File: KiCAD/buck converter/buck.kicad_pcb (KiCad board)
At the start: 2 copper layers, 42.2 x 24.9 mm, 17 parts, among them P1 VIN, P2 VOUT, Q1 Q_PMOS_DGS, U1 LTC1771

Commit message: Updated schematic, PCB, amd BOM
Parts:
- removed JP1: BURST, Connectors:PINHEAD1-3
- removed Q1: Q_PMOS_DGS, TO_SOT_Packages_SMD:SOT-23-6_Handsoldering
- added U2: SI3421DV-T1-GE3, TO_SOT_Packages_SMD:SOT-23-6_Handsoldering, F.Cu at (134.4, 95.2)
- C4: value 150uF -> 330uF; footprint Capacitors_SMD:CP_Elec_6.3x5.8 -> Capacitors_SMD:CP_Elec_8x10
- D2: footprint Diodes_SMD:D_SOD-323_HandSoldering -> Diodes_SMD:D_SMA_Handsoldering
- moved C3 10.5 mm to (133.6, 107.9)
- moved R2 10.5 mm to (131.4, 108.0)
- moved R4 10.5 mm to (135.9, 108.0)
- moved C4 8.15 mm to (124.0, 109.2), turned to 0 degrees
- moved C2 7.57 mm to (136.1, 102.6)
- moved P1 7.42 mm to (113.3, 102.6)
- moved R1 7.23 mm to (127.5, 96.0)
- moved C5 6.60 mm to (126.5, 94.0)
- moved C6 6.42 mm to (118.2, 93.5)
- moved C1 3.44 mm to (125.5, 103.6)
- moved D2 2.90 mm to (133.1, 90.9), turned to 180 degrees
- moved R3 1.27 mm to (134.6, 102.2)
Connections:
- U1 pad 8: /MODE -> GND
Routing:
- net GND: track 21.8 -> 47.1 mm, vias 5 -> 4
- net /MODE: track 19.2 -> 0.00 mm, vias 2 -> 0
- net Vfb: track 22.2 -> 8.71 mm, vias 2 -> 0
- net /Ith: track 12.7 -> 5.87 mm
- net Net-(C2-Pad1): track 9.40 -> 2.85 mm, vias 2 -> 0
- net /SENSE: track 19.9 -> 14.5 mm, vias 3 -> 2
- net /RUN/SS: track 6.06 -> 2.19 mm
- net /GATE: track 5.61 -> 2.20 mm
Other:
- board text removed: "-"

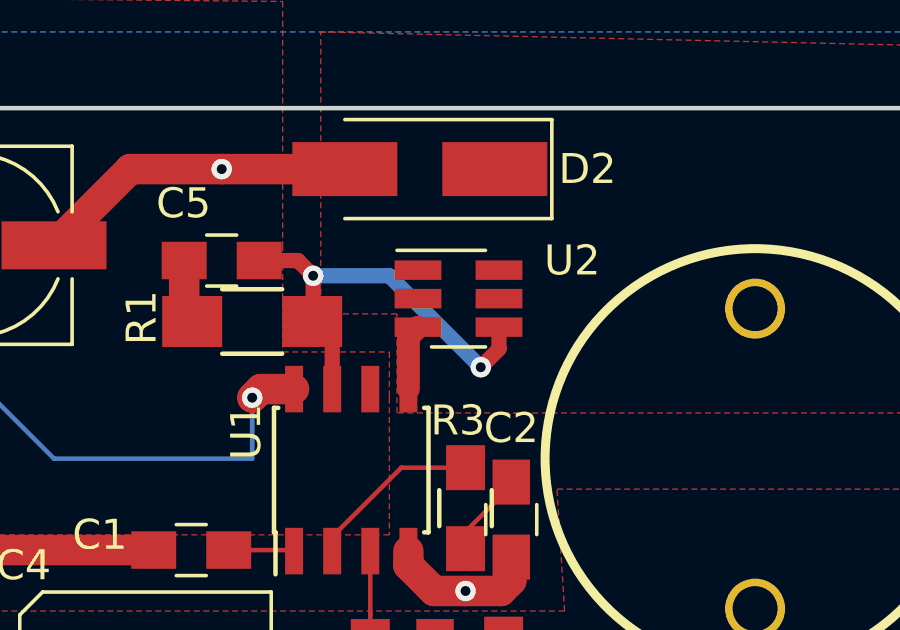
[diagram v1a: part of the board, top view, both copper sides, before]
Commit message: Updated PCB and SPICE
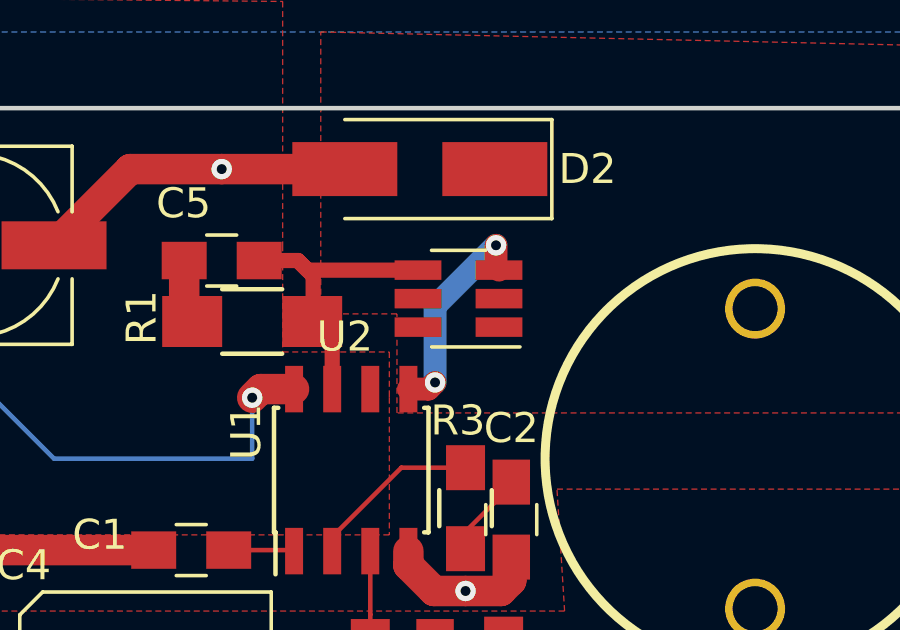
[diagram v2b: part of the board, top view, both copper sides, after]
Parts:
- turned U2 to 180 degrees
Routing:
- net /GATE: track 2.20 -> 7.26 mm, vias 0 -> 2
- net /SENSE: track 14.5 -> 10.2 mm, vias 2 -> 0
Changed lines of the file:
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@@
-(kicad_pcb (version 4) (host pcbnew 4.0.3-stable)
+(kicad_pcb (version 4) (host pcbnew 4.0.5)
   (general
     (links 32)
     (no_connects 0)
-    (area 109.652999 88.824999 151.967001 113.867001)
+    (area 106.68 82.14614 159.00642 114.300001)
     (thickness 1.6)
     (drawings 11)
-    (tracks 56)
+    (tracks 58)
     (zones 0)
     (modules 16)
@@
   )
   (module TO_SOT_Packages_SMD:SOT-23-6_Handsoldering (layer F.Cu)
-    (at 134.385122 95.25)
+    (at 134.385122 95.25 180)
     (descr "6-pin SOT-23 package, Handsoldering")
     (tags "SOT-23-6 Handsoldering")
     (attr smd)
-    (fp_text reference U2 (at 3.790878 -1.27) (layer F.SilkS)
-      (effects (font (size 1 1) (thickness 0.15)))
-    )
-    (fp_text value SI3421DV-T1-GE3 (at 0 2.9) (layer F.Fab) hide
-      (effects (font (size 1 1) (thickness 0.15)))
-    )
-    (fp_text user %R (at 0 -0.423001) (layer F.Fab)
+    (fp_text reference U2 (at 3.790878 -1.27 180) (layer F.SilkS)
+      (effects (font (size 1 1) (thickness 0.15)))
+    )
+    (fp_text value SI3421DV-T1-GE3 (at 0 2.9 180) (layer F.Fab) hide
+      (effects (font (size 1 1) (thickness 0.15)))
+    )
+    (fp_text user %R (at 0 -0.423001 180) (layer F.Fab)
       (effects (font (size 0.5 0.5) (thickness 0.075)))
     )
@@
     (fp_line (start 0.9 1.55) (end -0.9 1.55) (layer F.Fab) (width 0.1))
     (fp_line (start 0.9 -1.55) (end 0.9 1.55) (layer F.Fab) (width 0.1))
-    (pad 1 smd rect (at -1.35 -0.95) (size 1.56 0.65) (layers F.Cu F.Paste F.Mask)
+    (pad 1 smd rect (at -1.35 -0.95 180) (size 1.56 0.65) (layers F.Cu F.Paste F.Mask)
       (net 6 /Vsw))
-    (pad 2 smd rect (at -1.35 0) (size 1.56 0.65) (layers F.Cu F.Paste F.Mask)
+    (pad 2 smd rect (at -1.35 0 180) (size 1.56 0.65) (layers F.Cu F.Paste F.Mask)
       (net 6 /Vsw))
-    (pad 3 smd rect (at -1.35 0.95) (size 1.56 0.65) (layers F.Cu F.Paste F.Mask)
+    (pad 3 smd rect (at -1.35 0.95 180) (size 1.56 0.65) (layers F.Cu F.Paste F.Mask)
       (net 9 /GATE))
-    (pad 4 smd rect (at 1.35 0.95) (size 1.56 0.65) (layers F.Cu F.Paste F.Mask)
+    (pad 4 smd rect (at 1.35 0.95 180) (size 1.56 0.65) (layers F.Cu F.Paste F.Mask)
       (net 8 /SENSE))
-    (pad 6 smd rect (at 1.35 -0.95) (size 1.56 0.65) (layers F.Cu F.Paste F.Mask)
+    (pad 6 smd rect (at 1.35 -0.95 180) (size 1.56 0.65) (layers F.Cu F.Paste F.Mask)
       (net 6 /Vsw))
-    (pad 5 smd rect (at 1.35 0) (size 1.56 0.65) (layers F.Cu F.Paste F.Mask)
+    (pad 5 smd rect (at 1.35 0 180) (size 1.56 0.65) (layers F.Cu F.Paste F.Mask)
       (net 6 /Vsw))
     (model ${KISYS3DMOD}/TO_SOT_Packages_SMD.3dshapes/SOT-23-6.wrl
@@
   (segment (start 126.726 103.632) (end 128.872 103.632) (width 0.1524) (layer F.Cu) (net 7))
   (segment (start 128.872 103.632) (end 128.905 103.665) (width 0.1524) (layer F.Cu) (net 7))
+  (segment (start 133.035122 94.3) (end 129.352 94.3) (width 0.508) (layer F.Cu) (net 8))
+  (segment (start 129.352 94.3) (end 129.032 93.98) (width 0.508) (layer F.Cu) (net 8))
   (segment (start 127.742 93.98) (end 129.032 93.98) (width 0.508) (layer F.Cu) (net 8))
   (segment (start 129.032 93.98) (end 129.54 94.488) (width 0.508) (layer F.Cu) (net 8))
@@
   (segment (start 129.54 94.488) (end 129.54 95.98) (width 0.508) (layer F.Cu) (net 8))
   (segment (start 129.54 95.98) (end 129.508 96.012) (width 0.508) (layer F.Cu) (net 8))
-  (segment (start 135.128 97.536) (end 132.08 94.488) (width 0.508) (layer B.Cu) (net 8))
-  (segment (start 132.08 94.488) (end 129.54 94.488) (width 0.508) (layer B.Cu) (net 8))
-  (via (at 129.54 94.488) (size 0.6858) (drill 0.3302) (layers F.Cu B.Cu) (net 8))
-  (segment (start 135.735122 96.2) (end 135.735122 96.928878) (width 0.508) (layer F.Cu) (net 8))
-  (segment (start 135.735122 96.928878) (end 135.128 97.536) (width 0.508) (layer F.Cu) (net 8))
-  (via (at 135.128 97.536) (size 0.6858) (drill 0.3302) (layers F.Cu B.Cu) (net 8))
-  (segment (start 132.715 98.265) (end 132.715 96.520122) (width 0.762) (layer F.Cu) (net 9))
-  (segment (start 132.715 96.520122) (end 133.035122 96.2) (width 0.762) (layer F.Cu) (net 9))
+  (segment (start 135.636 93.472) (end 135.636 94.200878) (width 0.762) (layer F.Cu) (net 9))
+  (segment (start 135.636 94.200878) (end 135.735122 94.3) (width 0.762) (layer F.Cu) (net 9))
+  (segment (start 133.604 98.044) (end 133.604 95.504) (width 0.762) (layer B.Cu) (net 9))
+  (segment (start 133.604 95.504) (end 135.636 93.472) (width 0.762) (layer B.Cu) (net 9))
+  (via (at 135.636 93.472) (size 0.6858) (drill 0.3302) (layers F.Cu B.Cu) (net 9))
+  (segment (start 132.715 98.265) (end 133.383 98.265) (width 0.762) (layer F.Cu) (net 9))
+  (segment (start 133.383 98.265) (end 133.604 98.044) (width 0.762) (layer F.Cu) (net 9))
+  (via (at 133.604 98.044) (size 0.6858) (drill 0.3302) (layers F.Cu B.Cu) (net 9))
   (segment (start 134.62 100.885) (end 132.48 100.885) (width 0.1524) (layer F.Cu) (net 10))
   (segment (start 132.48 100.885) (end 130.175 103.19) (width 0.1524) (layer F.Cu) (net 10))

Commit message: Board design updated
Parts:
- added C7: 100nF, Capacitors_SMD:C_0805_HandSoldering, F.Cu at (124.5, 98.6)
- C4: value 330uF -> 150uF; footprint Capacitors_SMD:CP_Elec_8x10 -> Capacitors_SMD:CP_Elec_6.3x7.7
- C6: value 22uF -> 56uF; footprint Capacitors_SMD:CP_Elec_6.3x5.3 -> Capacitors_SMD:CP_Elec_5x5.7
- R1: value 20m -> 33m
- moved D2 3.30 mm to (129.8, 90.9)
- moved C4 0.60 mm to (123.3, 109.2)
- moved R1 0.51 mm to (128.0, 96.0)
- moved C6 0.18 mm to (118.0, 93.5)
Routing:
- net GND: track 47.1 -> 46.3 mm
- net /SENSE: track 10.2 -> 9.52 mm

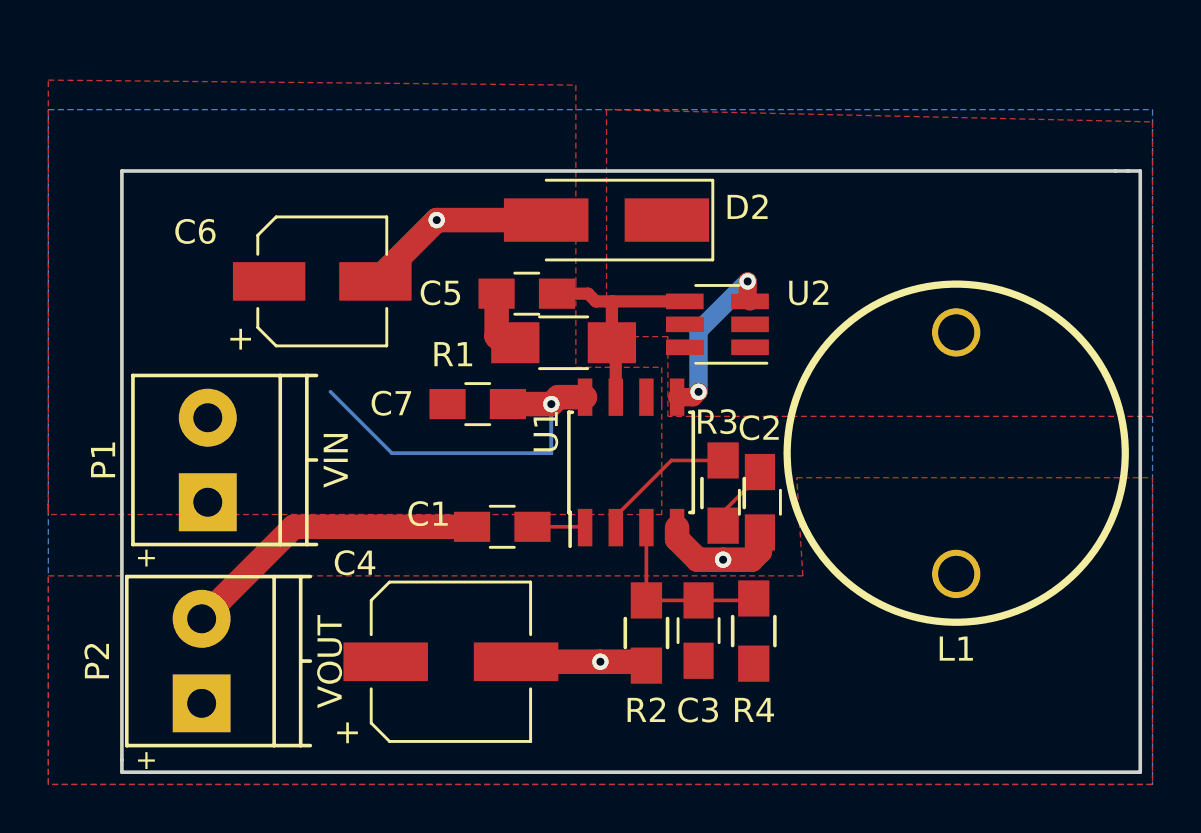
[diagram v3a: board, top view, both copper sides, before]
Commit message: updated board with via stitching
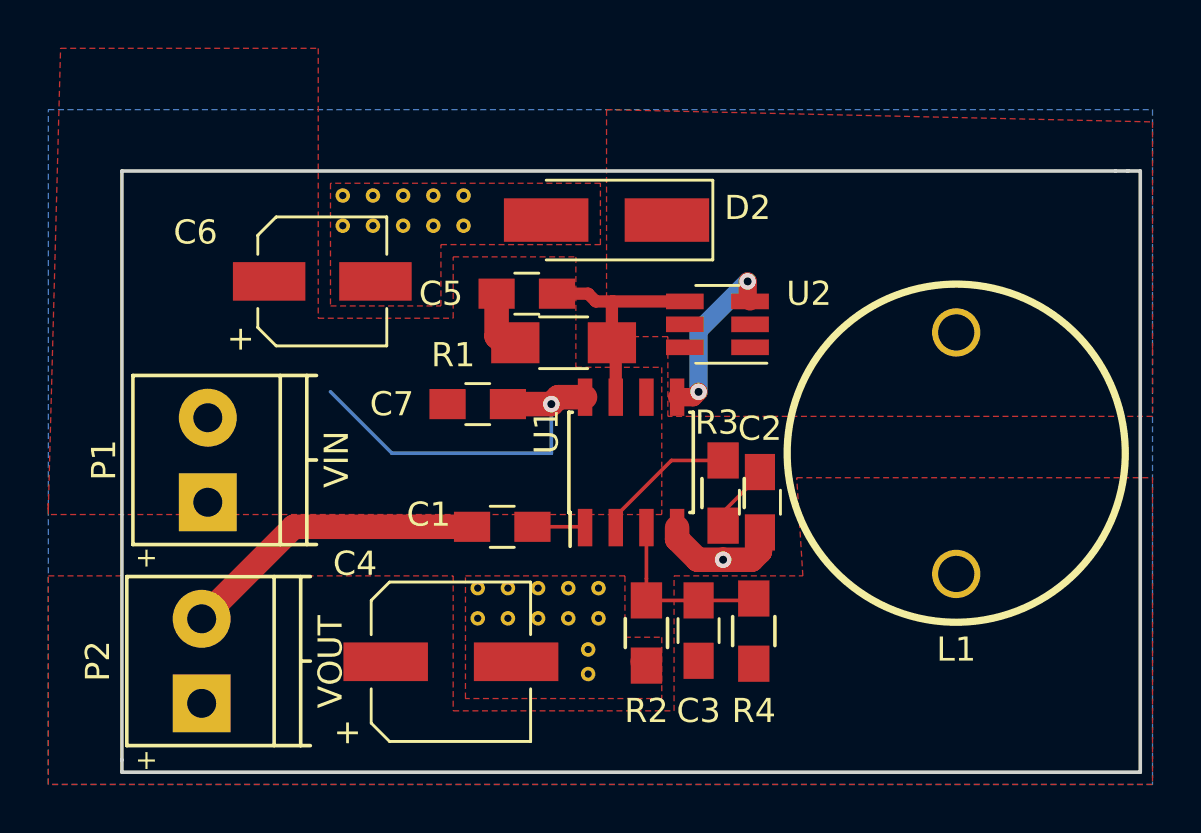
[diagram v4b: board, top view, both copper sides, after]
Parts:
- added REF**: via0.6mm, Via_Stitch:via0.6mm, F.Cu at (129.0, 109.7)
- added REF**: via0.6mm, Via_Stitch:via0.6mm, F.Cu at (127.0, 106.2)
- added REF**: via0.6mm, Via_Stitch:via0.6mm, F.Cu at (125.7, 106.2)
- added REF**: via0.6mm, Via_Stitch:via0.6mm, F.Cu at (124.5, 106.2)
- added REF**: via0.6mm, Via_Stitch:via0.6mm, F.Cu at (123.9, 91.2)
- added REF**: via0.6mm, Via_Stitch:via0.6mm, F.Cu at (122.6, 91.2)
- added REF**: via0.6mm, Via_Stitch:via0.6mm, F.Cu at (121.4, 91.2)
- added REF**: via0.6mm, Via_Stitch:via0.6mm, F.Cu at (120.1, 91.2)
- added REF**: via0.6mm, Via_Stitch:via0.6mm, F.Cu at (118.9, 91.2)
- added REF**: via0.6mm, Via_Stitch:via0.6mm, F.Cu at (123.9, 89.9)
- added REF**: via0.6mm, Via_Stitch:via0.6mm, F.Cu at (122.6, 89.9)
- added REF**: via0.6mm, Via_Stitch:via0.6mm, F.Cu at (129.0, 108.7)
- added REF**: via0.6mm, Via_Stitch:via0.6mm, F.Cu at (121.4, 89.9)
- added REF**: via0.6mm, Via_Stitch:via0.6mm, F.Cu at (120.1, 89.9)
- added REF**: via0.6mm, Via_Stitch:via0.6mm, F.Cu at (118.9, 89.9)
- added REF**: via0.6mm, Via_Stitch:via0.6mm, F.Cu at (129.5, 107.4)
- added REF**: via0.6mm, Via_Stitch:via0.6mm, F.Cu at (128.2, 107.4)
- added REF**: via0.6mm, Via_Stitch:via0.6mm, F.Cu at (127.0, 107.4)
- added REF**: via0.6mm, Via_Stitch:via0.6mm, F.Cu at (125.7, 107.4)
- added REF**: via0.6mm, Via_Stitch:via0.6mm, F.Cu at (124.5, 107.4)
- added REF**: via0.6mm, Via_Stitch:via0.6mm, F.Cu at (129.5, 106.2)
- added REF**: via0.6mm, Via_Stitch:via0.6mm, F.Cu at (128.2, 106.2)
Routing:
- net GND: track 46.3 -> 33.9 mm, vias 4 -> 2
- added copper zone on F.Cu, net GND
